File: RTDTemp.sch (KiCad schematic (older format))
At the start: 92 parts, among them J11 Conn_01x02, J4 CAN_In, J5 CAN_Out, U2 Nucleo_L432KC, U3 PDS1-Sx-Sx, U5 ADM3055E, U7 CDSOT23-T24CAN

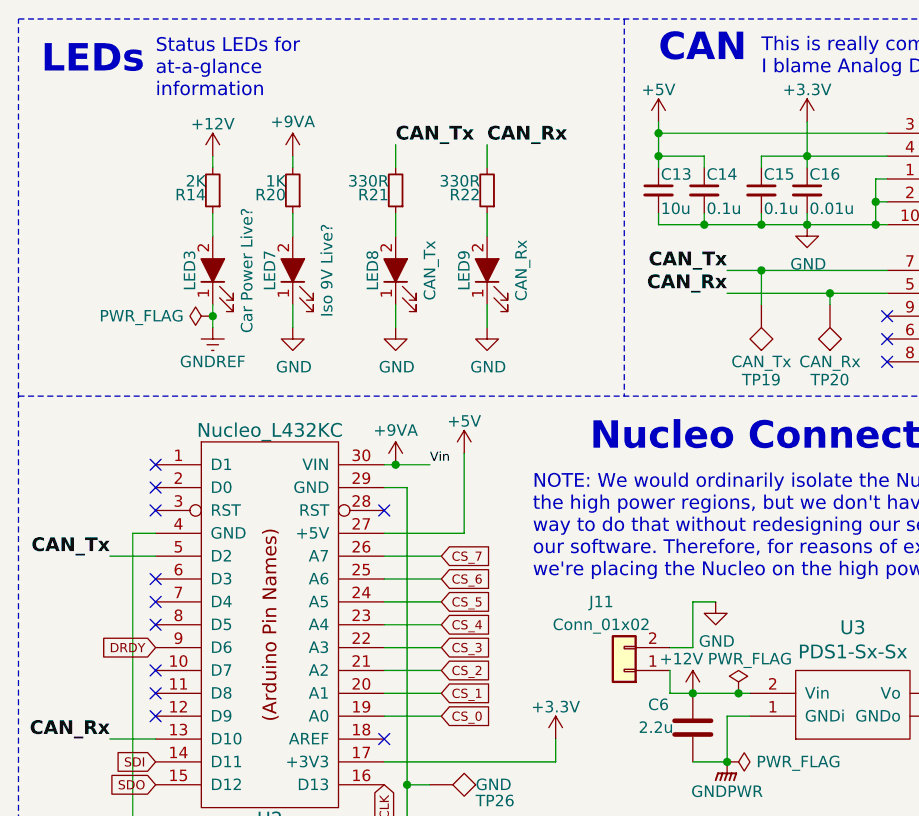
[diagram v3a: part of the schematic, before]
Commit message: Arragned Board
Arragned Board, room for optimization
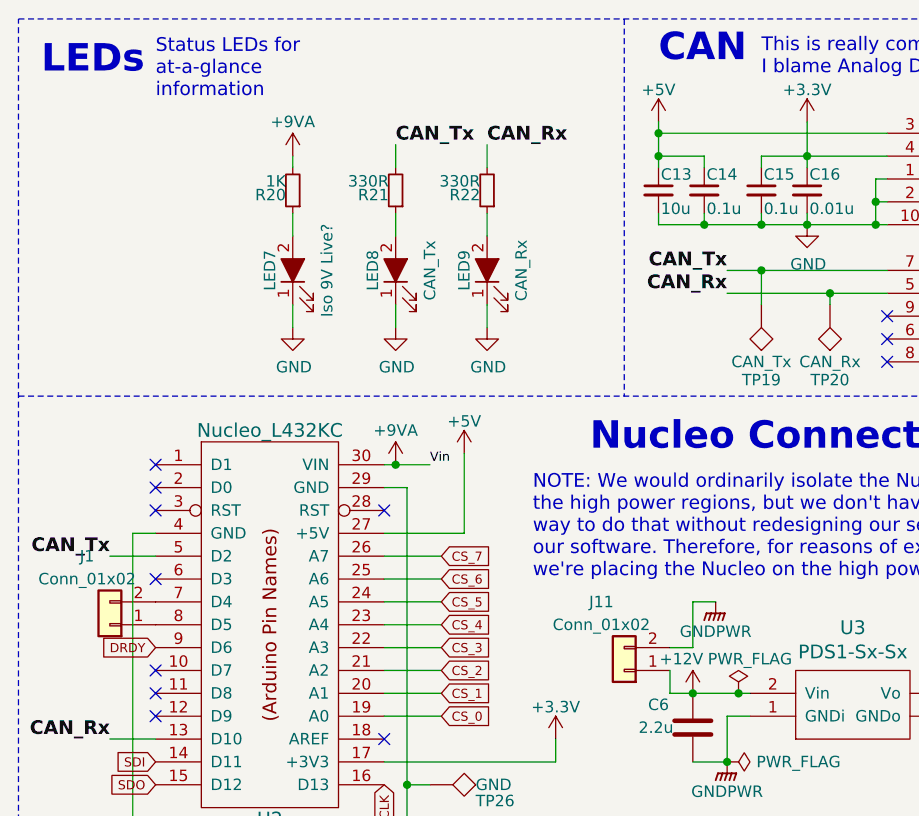
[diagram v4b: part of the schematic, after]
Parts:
- removed LED3: Car Power Live?, LED_SMD:LED_0805_2012Metric, symbol RTDTemp-rescue:LED_ALT-MPPT-rescue
- removed R14: 2K, Resistor_SMD:R_0805_2012Metric, symbol RTDTemp-rescue:R_Small-MPPT-rescue
- added J1: Conn_01x02, Connector_Molex:Molex_Micro-Fit_3.0_43650-0215_1x02_P3.00mm_Vertical, symbol Connector_Generic:Conn_01x02
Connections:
- net GND: no longer J11.2 (Pin_2)
- net GNDPWR: now also J11.2 (Pin_2)
- net at U2.7 (D4): now also J1.2 (Pin_2)
- net at U2.8 (D5): now also J1.1 (Pin_1)
- no-connect marks 15 -> 13
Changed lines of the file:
@@
 Text Label 1000 3700 2    60   ~ 12
 CAN_Rx
-NoConn ~ 1200 2500
-NoConn ~ 1200 2600
 NoConn ~ 1200 3400
 NoConn ~ 1200 3500
@@
 Text Notes 1200 900  0    60   ~ 0
 Status LEDs for\nat-a-glance\ninformation
-$Comp
-L RTDTemp-rescue:LED_ALT-MPPT-rescue LED3
-U 1 1 5BC3DA9B
-P 1450 1650
-F 0 "LED3" H 1450 1750 50  0000 C CNN
-F 1 "Car Power Live?" H 1450 1500 50  0000 C CNN
-F 2 "LED_SMD:LED_0805_2012Metric" H 1450 1650 50  0001 C CNN
-F 3 "" H 1450 1650 50  0001 C CNN
-	1    1450 1650
-	0    -1   -1   0
-$EndComp
-$Comp
-L RTDTemp-rescue:R_Small-MPPT-rescue R14
-U 1 1 5BC3DAA7
-P 1450 1300
-F 0 "R14" H 1480 1320 50  0000 L CNN
-F 1 "2K" H 1480 1260 50  0000 L CNN
-F 2 "Resistor_SMD:R_0805_2012Metric" H 1450 1300 50  0001 C CNN
-F 3 "" H 1450 1300 50  0001 C CNN
-	1    1450 1300
-	-1   0    0    1
-$EndComp
 $Comp
 L RTDTemp-rescue:LED_ALT-MPPT-rescue LED7
@@
 $EndComp
 $Comp
-L RTDTemp-rescue:GNDREF-MPPT-rescue #PWR041
-U 1 1 5BC77E73
-P 1450 1900
-F 0 "#PWR041" H 1450 1650 50  0001 C CNN
-F 1 "GNDREF" H 1450 1750 50  0000 C CNN
-F 2 "" H 1450 1900 50  0001 C CNN
-F 3 "" H 1450 1900 50  0001 C CNN
-	1    1450 1900
-	1    0    0    -1
-$EndComp
-$Comp
-L RTDTemp-rescue:+12V-MPPT-rescue #PWR042
-U 1 1 5BC781A9
-P 1450 1150
-F 0 "#PWR042" H 1450 1000 50  0001 C CNN
-F 1 "+12V" H 1450 1290 50  0000 C CNN
-F 2 "" H 1450 1150 50  0001 C CNN
-F 3 "" H 1450 1150 50  0001 C CNN
-	1    1450 1150
-	1    0    0    -1
-$EndComp
-$Comp
 L RTDTemp-rescue:LED_ALT-MPPT-rescue LED8
 U 1 1 5BC7B329
@@
 	1000 3700 1200 3700
 Wire Wire Line
-	1000 2900 1200 2900
-Wire Wire Line
 	5850 2100 5800 2100
 Wire Wire Line
@@
 	2650 1200 2650 1100
 Wire Wire Line
-	1450 1900 1450 1850
-Wire Wire Line
-	1450 1500 1450 1400
-Wire Wire Line
-	1450 1200 1450 1150
-Wire Wire Line
 	1800 1150 1800 1200
 Wire Wire Line
@@
 Wire Wire Line
 	6150 2100 6200 2100
-$Comp
-L RTDTemp-rescue:Nucleo_L432KC-MPPT-rescue U2
-U 1 1 5BBBD3B0
-P 1700 3200
-F 0 "U2" H 1700 2350 60  0000 C CNN
-F 1 "Nucleo_L432KC" H 1700 4050 60  0000 C CNN
-F 2 "UTSVT_Special:NucleoL432KC" H 1700 2900 60  0001 C CNN
-F 3 "" H 1700 2900 60  0001 C CNN
-	1    1700 3200
-	1    0    0    -1
-$EndComp
 $Comp
 L RTDTemp-rescue:TEST-MPPT-rescue TP26
@@
 Wire Wire Line
 	2450 2900 2200 2900
-$Comp
-L RTDTemp-rescue:PWR_FLAG-MPPT-rescue #FLG0105
-U 1 1 5F3734A8
-P 1450 1850
-F 0 "#FLG0105" H 1450 1925 50  0001 C CNN
-F 1 "PWR_FLAG" V 1450 1977 50  0000 L CNN
-F 2 "" H 1450 1850 50  0001 C CNN
-F 3 "" H 1450 1850 50  0001 C CNN
-	1    1450 1850
-	0    -1   -1   0
-$EndComp
-Connection ~ 1450 1850
-Wire Wire Line
-	1450 1850 1450 1800
 Connection ~ 2300 3900
 Wire Wire Line
@@
 Wire Wire Line
 	5000 3500 5150 3500
-$Comp
-L RTDTemp-rescue:PDS1-Sx-Sx-utsvt-power-regulators U3
-U 1 1 5EB6D889
-P 4250 3550
-F 0 "U3" H 4250 3887 60  0000 C CNN
-F 1 "PDS1-Sx-Sx" H 4250 3781 60  0000 C CNN
-F 2 "UTSVT_ICs:PDSx-S" H 4250 3500 60  0001 C CNN
-F 3 "" H 4250 3500 60  0001 C CNN
-	1    4250 3550
-	1    0    0    -1
-$EndComp
 Connection ~ 4700 3500
 Wire Wire Line
@@
 Wire Wire Line
 	3450 3400 3450 3500
-$Comp
-L power:GND #PWR0103
-U 1 1 5E5C95E9
-P 3650 3100
-F 0 "#PWR0103" H 3650 2850 50  0001 C CNN
-F 1 "GND" H 3655 2927 50  0000 C CNN
-F 2 "" H 3650 3100 50  0001 C CNN
-F 3 "" H 3650 3100 50  0001 C CNN
-	1    3650 3100
-	1    0    0    -1
-$EndComp
-Wire Wire Line
-	1100 2800 1200 2800
 Wire Wire Line
 	1100 4050 1100 2800
 Wire Wire Line
 	2550 2450 2550 2800
-NoConn ~ 1200 2700
 NoConn ~ 2200 2700
 Text Label 1000 2900 2    60   ~ 12
 CAN_Tx
-NoConn ~ 1200 3200
 Wire Wire Line
 	3550 3300 3550 3100
@@
 Text GLabel 1200 3300 0    40   Input ~ 0
 DRDY
-NoConn ~ 1200 3100
 Text GLabel 1200 3800 0    40   Input ~ 0
 SDI
@@
 Text GLabel 2450 2900 2    40   Input ~ 0
 CS_7
-NoConn ~ 1200 3000
 Text GLabel 2450 3000 2    40   Input ~ 0
 CS_6
@@
 Text GLabel 3800 14450 0    40   Input ~ 0
 CS_6
+$Comp
+L RTDTemp-rescue:PDS1-Sx-Sx-utsvt-power-regulators U3
+U 1 1 5EB6D889
+P 4250 3550
+F 0 "U3" H 4250 3887 60  0000 C CNN
+F 1 "PDS1-Sx-Sx" H 4250 3781 60  0000 C CNN
+F 2 "UTSVT_ICs:PDSx-S" H 4250 3500 60  0001 C CNN
+F 3 "" H 4250 3500 60  0001 C CNN
+	1    4250 3550
+	1    0    0    -1
+$EndComp
+$Comp
+L Connector_Generic:Conn_01x02 J1
+U 1 1 5FD57E19
+P 1000 3200
+F 0 "J1" H 1100 2900 50  0000 C CNN
+F 1 "Conn_01x02" H 1100 3000 50  0000 C CNN
+F 2 "Connector_Molex:Molex_Micro-Fit_3.0_43650-0215_1x02_P3.00mm_Vertical" H 1000 3200 50  0001 C CNN
+F 3 "~" H 1000 3200 50  0001 C CNN
+	1    1000 3200
+	-1   0    0    1
+$EndComp
+NoConn ~ 1200 3000
+NoConn ~ 1200 2700
+Wire Wire Line
+	1100 2800 1200 2800
+$Comp
+L RTDTemp-rescue:Nucleo_L432KC-MPPT-rescue U2
+U 1 1 5BBBD3B0
+P 1700 3200
+F 0 "U2" H 1700 2350 60  0000 C CNN
+F 1 "Nucleo_L432KC" H 1700 4050 60  0000 C CNN
+F 2 "UTSVT_Special:NucleoL432KC" H 1700 2900 60  0001 C CNN
+F 3 "" H 1700 2900 60  0001 C CNN
+	1    1700 3200
+	1    0    0    -1
+$EndComp
+Wire Wire Line
+	1000 2900 1200 2900
+NoConn ~ 1200 2500
+NoConn ~ 1200 2600
+$Comp
+L RTDTemp-rescue:GNDPWR-MPPT-rescue #PWR0103
+U 1 1 5FE403E5
+P 3650 3100
+F 0 "#PWR0103" H 3650 2900 50  0001 C CNN
+F 1 "GNDPWR" H 3650 2970 50  0000 C CNN
+F 2 "" H 3650 3050 50  0001 C CNN
+F 3 "" H 3650 3050 50  0001 C CNN
+	1    3650 3100
+	1    0    0    -1
+$EndComp
 $EndSCHEMATC

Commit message: PR ready RTD/Irradiance Sensor Board. Added extra mounts for irradiance I2C and updated power reg to match MPPT. Also cleaner layout.
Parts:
- removed C6: 2.2u, Capacitor_SMD:C_0805_2012Metric, symbol Device:C
- removed C7: 4.7u, Capacitor_SMD:C_0805_2012Metric, symbol Device:C
- removed J11: Conn_01x02, Connector_Molex:Molex_Micro-Fit_3.0_43650-0215_1x02_P3.00mm_Vertical, symbol Connector_Generic:Conn_01x02
- removed RTD0_C0, RTD0_C1, RTD0_C2, RTD1_C0, RTD1_C1, RTD1_C2, RTD2_C0, RTD2_C1, RTD2_C2, RTD3_C0, RTD3_C1, RTD3_C2, RTD4_C0, RTD4_C1, RTD4_C2, RTD5_C0, RTD5_C1, RTD5_C2, RTD6_C0, RTD6_C1, RTD6_C2, RTD7_C0, RTD7_C1, RTD7_C2: 100nF, Capacitor_SMD:C_0805_2012Metric, symbol Device:C_Small
- removed RTD0_J0, RTD1_J0, RTD2_J0, RTD3_J0, RTD4_J0, RTD5_J0, RTD6_J0, RTD7_J0: Conn_01x04, Connector_Molex:Molex_Micro-Fit_3.0_43650-0415_1x04_P3.00mm_Vertical, symbol Connector_Generic:Conn_01x04
- removed RTD0_R0, RTD1_R0, RTD2_R0, RTD3_R0, RTD4_R0, RTD5_R0, RTD6_R0, RTD7_R0: 400, Resistor_SMD:R_0805_2012Metric, symbol Device:R_Small
- removed RTD0_U0, RTD1_U0, RTD2_U0, RTD3_U0, RTD4_U0, RTD5_U0, RTD6_U0, RTD7_U0: MAX31865xAP, Package_SO:SSOP-20_5.3x7.2mm_P0.65mm, symbol Sensor_Temperature:MAX31865xAP
- removed TP26: GND, TestPoint:TestPoint_Keystone_5005-5009_Compact, symbol RTDTemp-rescue:TEST-MPPT-rescue
- removed U3: PDS1-Sx-Sx, UTSVT_ICs:PDSx-S, symbol RTDTemp-rescue:PDS1-Sx-Sx-utsvt-power-regulators
- added C1, C4: 100uF, Capacitor_SMD:C_1210_3225Metric, symbol Device:CP1_Small
- added C2: 47uF, Capacitor_SMD:C_1210_3225Metric, symbol Device:CP1_Small
- added C3: 10uF, Capacitor_SMD:C_0805_2012Metric, symbol Device:C_Small
- added J2: Conn_01x02, Connector_Molex:Molex_Micro-Fit_3.0_43650-0215_1x02_P3.00mm_Vertical, symbol Connector_Generic:Conn_01x02
- added J3: Car Power, Connector_Molex:Molex_Micro-Fit_3.0_43650-0215_1x02_P3.00mm_Vertical, symbol Array:PWR_Connector_43650-0215
- added L1: 4.7uH, Inductor_SMD:L_0805_2012Metric, symbol Device:L_Small
- added LED1: Car Power Live (Green), LED_SMD:LED_0805_2012Metric, symbol Device:LED_ALT
- added LED5: Tracking (Blue), LED_SMD:LED_0805_2012Metric, symbol Device:LED_ALT
- added LED6: Error (Amber), LED_SMD:LED_0805_2012Metric, symbol Device:LED_ALT
- added R1, R2: 4.7k, Resistor_SMD:R_0805_2012Metric, symbol Device:R
- added R3: 1.5K, Resistor_SMD:R_0805_2012Metric, symbol Device:R_Small
- added R7, R8: 330, Resistor_SMD:R_0805_2012Metric, symbol Device:R_Small
- added SW1: SW_Push, Button_Switch_THT:SW_PUSH_6mm, symbol Switch:SW_Push
- added TP2: Car +12V, TestPoint:TestPoint_Keystone_5005-5009_Compact, symbol Connector:TestPoint
- added TP3: Car GND, TestPoint:TestPoint_Keystone_5005-5009_Compact, symbol Connector:TestPoint
- added TP4: +9VA, TestPoint:TestPoint_Keystone_5005-5009_Compact, symbol Connector:TestPoint
- added TP5: GNDP, TestPoint:TestPoint_Keystone_5005-5009_Compact, symbol Connector:TestPoint
- added U2: PWR_REG_PQMC3-Dx-Sx-S, Array-RTDPCB:490_PQMC3_D12_S12_S, symbol Array:PWR_REG_PQMC3-Dx-Sx-S
- C10: renamed from C9; value 10u -> 10uF; symbol RTDTemp-rescue:C_Small-MPPT-rescue -> Device:C_Small
- C11: value 0.1u -> 0.01uF; symbol RTDTemp-rescue:C_Small-MPPT-rescue -> Device:C_Small
- C12: value 0.01u -> 0.1uF; symbol RTDTemp-rescue:C_Small-MPPT-rescue -> Device:C_Small
- C5: renamed from C13; value 10u -> 10uF; symbol RTDTemp-rescue:C_Small-MPPT-rescue -> Device:C_Small
- C6: renamed from C14; value 0.1u -> 0.1uF; symbol RTDTemp-rescue:C_Small-MPPT-rescue -> Device:C_Small
- C7: renamed from C15; value 0.1u -> 0.1uF; symbol RTDTemp-rescue:C_Small-MPPT-rescue -> Device:C_Small
- C8: renamed from C16; value 0.01u -> 0.01uF; symbol RTDTemp-rescue:C_Small-MPPT-rescue -> Device:C_Small
- C9: renamed from C10; value 0.22u -> 0.22uF; symbol RTDTemp-rescue:C_Small-MPPT-rescue -> Device:C_Small
- J4, J5: footprint UTSVT_Connectors:Molex_MicroFit3.0_1x4xP3.00mm_PolarizingPeg_Vertical -> Connector_Molex:Molex_Micro-Fit_3.0_43650-0415_1x04_P3.00mm_Vertical; symbol RTDTemp-rescue:CANConnector-MPPT-rescue -> Array:CAN_Connector_43650-0427
- JP1: symbol RTDTemp-rescue:Jumper_NO_Small-MPPT-rescue -> Device:Jumper_NO_Small
- L2, L3: value 2k -> 1.8kH; symbol RTDTemp-rescue:Ferrite_Bead_Small-MPPT-rescue -> Device:Ferrite_Bead_Small
- LED2: renamed from LED7; value Iso 9V Live? -> Device 9V Live (Green); symbol RTDTemp-rescue:LED_ALT-MPPT-rescue -> Device:LED_ALT
- LED3: renamed from LED9; value CAN_Rx -> CAN_Rx (Blue); symbol RTDTemp-rescue:LED_ALT-MPPT-rescue -> Device:LED_ALT
- LED4: renamed from LED8; value CAN_Tx -> CAN_Tx (Blue); symbol RTDTemp-rescue:LED_ALT-MPPT-rescue -> Device:LED_ALT
- R10: symbol RTDTemp-rescue:R-MPPT-rescue -> Device:R
- R11: renamed from R9; symbol RTDTemp-rescue:R-MPPT-rescue -> Device:R
- R4: renamed from R20; value 1K -> 1.1K; symbol RTDTemp-rescue:R_Small-MPPT-rescue -> Device:R_Small
- R5: renamed from R22; value 330R -> 330; symbol RTDTemp-rescue:R_Small-MPPT-rescue -> Device:R_Small
- R6: renamed from R21; value 330R -> 330; symbol RTDTemp-rescue:R_Small-MPPT-rescue -> Device:R_Small
- R9: renamed from R25; symbol RTDTemp-rescue:R-MPPT-rescue -> Device:R
- TP10: renamed from TP15; symbol RTDTemp-rescue:TEST-MPPT-rescue -> Connector:TestPoint
- TP11: renamed from TP16; symbol RTDTemp-rescue:TEST-MPPT-rescue -> Connector:TestPoint
- TP12: renamed from TP21; symbol RTDTemp-rescue:TEST-MPPT-rescue -> Connector:TestPoint
- TP13: renamed from TP22; symbol RTDTemp-rescue:TEST-MPPT-rescue -> Connector:TestPoint
- TP6: renamed from TP19; symbol RTDTemp-rescue:TEST-MPPT-rescue -> Connector:TestPoint
- TP7: renamed from TP20; symbol RTDTemp-rescue:TEST-MPPT-rescue -> Connector:TestPoint
- TP8: renamed from TP13; symbol RTDTemp-rescue:TEST-MPPT-rescue -> Connector:TestPoint
- TP9: renamed from TP14; symbol RTDTemp-rescue:TEST-MPPT-rescue -> Connector:TestPoint
- U1: renamed from U2; footprint UTSVT_Special:NucleoL432KC -> Array-RTDPCB:MODULE_NUCLEO-L432KC; symbol RTDTemp-rescue:Nucleo_L432KC-MPPT-rescue -> Array:MCU_Nucleo_L432KC
- U3: renamed from U5; footprint UTSVT_ICs:SOIC-20W_7.5x15.4mm_Pitch1.27mm -> Array-RTDPCB:ADM3055EBRIZ; symbol RTDTemp-rescue:ADM3055E-MPPT-rescue -> Array:CAN_Chip_ADM3055E
- U4: renamed from U7; footprint Package_TO_SOT_SMD:SOT-23W_Handsoldering -> Package_TO_SOT_SMD:SOT-23; symbol RTDTemp-rescue:CDSOT23-T24CAN-MPPT-rescue -> Array:CAN_Bus_Protector_CDSOT23-T24CAN
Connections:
- net GND is gone; now on net GNDPWR: C5.2, C6.2, C7.2, C8.2, LED2.1 (K), LED3.1 (K), LED4.1 (K), U1.29 (GND), U1.4 (GND), U3.1 (GND_In), U3.10 (GND_In), U3.2 (GND_In)
- net +12V: now also C1.1, J3.1 (+12V), L1.1, R3.2, TP2.1
- net +3V3: now also R1.2, R2.2
- net +9VA: now also C4.1, TP4.1, U2.6 (+Vo)
- net CS_0: now also U1.20 (A1); no longer U1.19 (A0)
- net CS_1: now also U1.19 (A0); no longer U1.20 (A1)
- net CS_2: now also U1.11 (D8); no longer U1.21 (A2)
- net CS_3: now also U1.12 (D9); no longer U1.22 (A3)
- net CS_4: now also U1.22 (A3); no longer U1.23 (A4)
- net CS_5: now also U1.9 (D6); no longer U1.24 (A5)
- net CS_7: now also U1.6 (D3); no longer U1.26 (A7)
- net DRDY: now also U1.10 (D7); no longer U1.9 (D6)
- net GNDPWR: now also C3.1, C4.2, LED5.1 (K), LED6.1 (K), SW1.2, TP5.1, U2.7 (0V)
- net Reset: now reaches U1.28 (RST)
- net Reset: now also U1.3 (RST), SW1.1
- net at U1.7 (D4): now also J1.1 (Pin_1), J2.1 (Pin_1), R2.1; no longer J1.2 (Pin_2)
- net at U1.8 (D5): now also J1.2 (Pin_2), J2.2 (Pin_2), R1.1; no longer J1.1 (Pin_1)
- net at C11.1, C12.1, J4.1 (5V)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: now also C10.1; no longer C9.1
- net at C11.2, C12.2, J4.2 (GND)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: now also C10.2; no longer C9.2
- net at L2.2, TP8.1, U3.19 (V_ISO_Out): now also C9.1; no longer C10.1
- net at L3.2, TP11.1, U3.18 (GND_ISO_Out)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: now also C9.2; no longer C10.2
- new net: C2.1, L1.2, U2.2 (Vin)
- new net: C3.2, U2.8 (CS)
- new net: LED5.2 (A), R7.1
- new net: LED6.2 (A), R8.1
- new net: LED1.2 (A), R3.1
- new net Error: R8.2, U1.24 (A5)
- new net GNDREF: C1.2, C2.2, J3.2 (GND), LED1.1 (K), TP3.1, U2.1 (GND)
- new net Tracking: R7.2, U1.23 (A4)
- no-connect marks 13 -> 10
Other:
- note added: "Isolated Power Regions:\n* High Power/Nucleo\n - +9A, +5V, +3.3V\n - GNDPWR\n* Low Car Power\n - +12V\n - GNDREF"
- note added: "Note that A7 (PA2) and A2 (PA3) are reserved for STLink UART."
- note added: "Power Regulation"
- note added: "SCL"
- note added: "SDA"
- note removed: "NOTE: We would ordinarily isolate the Nucleo from\nthe high power regions, but we don't have a good\nway to do that without redesigning our sensors and\nour software. Therefore, for reasons of expediency,\nwe're placing the Nucleo on the high power plane."
- moved on the sheet: C10, C11, C12, C5, C6, C7, C8, C9, H1, H2, H3, H4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

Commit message: Addressed review.
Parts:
- TP5: value GNDP -> Device GND
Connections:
- net GNDPWR: now also C1.2, C2.2, J3.2 (GND), LED1.1 (K), TP3.1, U2.1 (GND); no longer C3.1, C4.2, C5.2, C6.2, C7.2, C8.2, LED2.1 (K), LED3.1 (K), LED4.1 (K), LED5.1 (K), LED6.1 (K), SW1.2, TP5.1, U1.29 (GND), U1.4 (GND), U2.7 (0V), U3.1 (GND_In), U3.10 (GND_In), U3.2 (GND_In)
- net GNDREF: now also C3.1, C4.2, C5.2, C6.2, C7.2, C8.2, LED2.1 (K), LED3.1 (K), LED4.1 (K), LED5.1 (K), LED6.1 (K), SW1.2, TP5.1, U1.29 (GND), U1.4 (GND), U2.7 (0V), U3.1 (GND_In), U3.10 (GND_In), U3.2 (GND_In); no longer C1.2, C2.2, J3.2 (GND), LED1.1 (K), TP3.1, U2.1 (GND)
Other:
- note added: "Isolated Power Regions:\n* Device/Board Power\n - +9VA, +5V, +3.3V\n - GNDREF\n* Car Power\n - +12V\n - GNDPWR"
- note removed: "Isolated Power Regions:\n* High Power/Nucleo\n - +9A, +5V, +3.3V\n - GNDPWR\n* Low Car Power\n - +12V\n - GNDREF"
- moved on the sheet: TP3, TP4, TP5

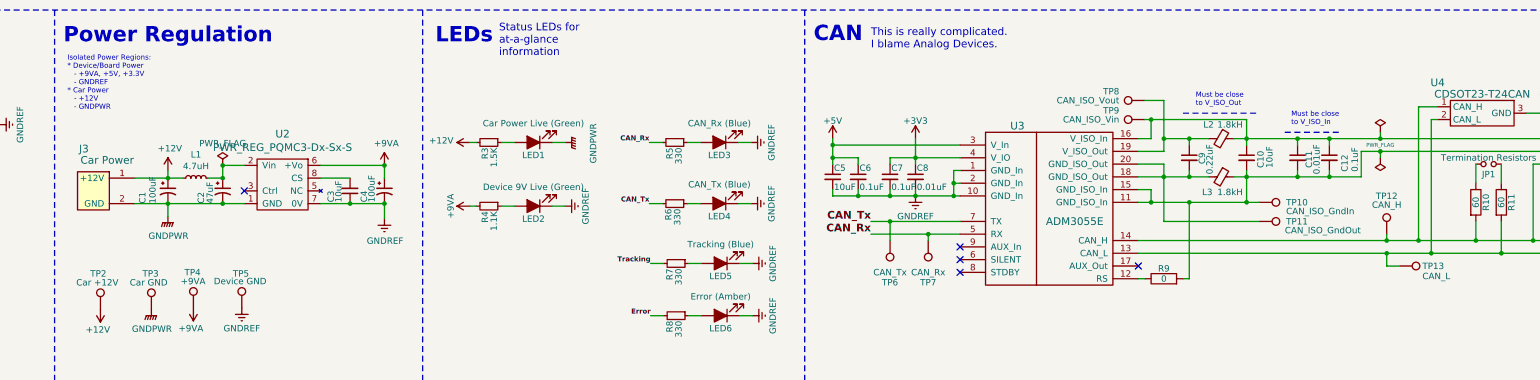
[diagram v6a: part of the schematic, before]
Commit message: Updated README with assembly and testing instructions.
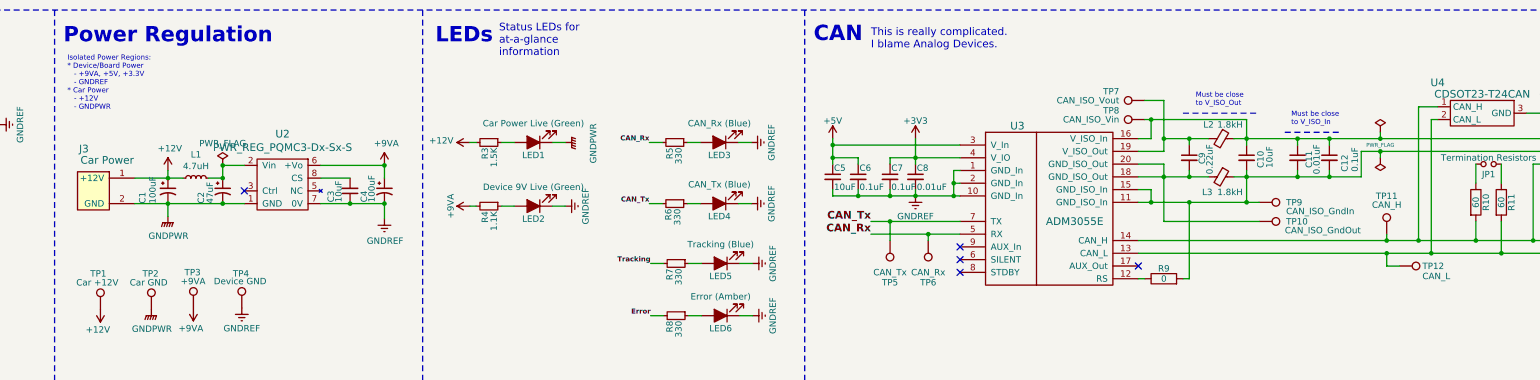
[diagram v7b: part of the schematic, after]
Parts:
- renumbered TP2 to TP1, TP11 to TP10, TP12 to TP11, TP13 to TP12, TP3 to TP2, TP4 to TP3, TP5 to TP4, TP6 to TP5, TP7 to TP6, TP8 to TP7, TP9 to TP8, TP10 to TP9
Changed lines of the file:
@@
 Sheet 1 9
 Title "UT SVT Irradiance/RTD Sensor Board"
-Date "2020-12-07"
+Date "2020-12-13"
 Rev "Rev1.0"
 Comp "UT Solar Vehicle Team"
 Comment1 "Jacob Giddens"
 Comment2 "Matthew Yu"
-Comment3 "Professor Gary Hallock"
+Comment3 "Gary Hallock"
 Comment4 ""
 $EndDescr
@@
 	15620 1610 15620 2210
 $Comp
-L Connector:TestPoint TP13
+L Connector:TestPoint TP12
 U 1 1 5BC9CD87
 P 14270 2610
-F 0 "TP13" V 14300 2790 50  0000 L BNN
+F 0 "TP12" V 14300 2790 50  0000 L BNN
 F 1 "CAN_L" V 14350 2790 50  0000 L CNN
 F 2 "TestPoint:TestPoint_Keystone_5005-5009_Compact" H 14270 2610 50  0001 C CNN
@@
 $EndComp
 $Comp
-L Connector:TestPoint TP12
+L Connector:TestPoint TP11
 U 1 1 5BC9CC23
 P 14170 2360
-F 0 "TP12" H 14170 2630 50  0000 C BNN
+F 0 "TP11" H 14170 2630 50  0000 C BNN
 F 1 "CAN_H" H 14170 2590 50  0000 C CNN
 F 2 "TestPoint:TestPoint_Keystone_5005-5009_Compact" H 14170 2360 50  0001 C CNN
@@
 $EndComp
 $Comp
-L Connector:TestPoint TP6
+L Connector:TestPoint TP5
 U 1 1 5BC87E62
 P 10270 2410
-F 0 "TP6" H 10270 2710 50  0000 C BNN
+F 0 "TP5" H 10270 2710 50  0000 C BNN
 F 1 "CAN_Tx" H 10270 2660 50  0000 C CNN
 F 2 "TestPoint:TestPoint_Keystone_5005-5009_Compact" H 10270 2410 50  0001 C CNN
@@
 $EndComp
 $Comp
-L Connector:TestPoint TP7
+L Connector:TestPoint TP6
 U 1 1 5BC87942
 P 10570 2410
-F 0 "TP7" H 10570 2710 50  0000 C BNN
+F 0 "TP6" H 10570 2710 50  0000 C BNN
 F 1 "CAN_Rx" H 10570 2660 50  0000 C CNN
 F 2 "TestPoint:TestPoint_Keystone_5005-5009_Compact" H 10570 2410 50  0001 C CNN
@@
 $EndComp
 $Comp
-L Connector:TestPoint TP8
+L Connector:TestPoint TP7
 U 1 1 5BC269CB
 P 12270 1310
-F 0 "TP8" V 12370 1510 50  0000 L BNN
+F 0 "TP7" V 12370 1510 50  0000 L BNN
 F 1 "CAN_ISO_Vout" V 12270 1510 50  0000 L CNN
 F 2 "TestPoint:TestPoint_Keystone_5005-5009_Compact" H 12270 1310 50  0001 C CNN
@@
 $EndComp
 $Comp
-L Connector:TestPoint TP10
+L Connector:TestPoint TP9
 U 1 1 5BC242A0
 P 13170 2110
-F 0 "TP10" V 13200 2320 50  0000 L BNN
+F 0 "TP9" V 13200 2320 50  0000 L BNN
 F 1 "CAN_ISO_GndIn" V 13240 2320 50  0000 L CNN
 F 2 "TestPoint:TestPoint_Keystone_5005-5009_Compact" H 13170 2110 50  0001 C CNN
@@
 $EndComp
 $Comp
-L Connector:TestPoint TP11
+L Connector:TestPoint TP10
 U 1 1 5BC2391E
 P 13170 2260
-F 0 "TP11" V 13200 2470 50  0000 L BNN
+F 0 "TP10" V 13200 2470 50  0000 L BNN
 F 1 "CAN_ISO_GndOut" V 13240 2460 50  0000 L CNN
 F 2 "TestPoint:TestPoint_Keystone_5005-5009_Compact" H 13170 2260 50  0001 C CNN
@@
 $EndComp
 $Comp
-L Connector:TestPoint TP9
+L Connector:TestPoint TP8
 U 1 1 5BC226FB
 P 12270 1460
-F 0 "TP9" V 12370 1660 50  0000 L BNN
+F 0 "TP8" V 12370 1660 50  0000 L BNN
 F 1 "CAN_ISO_Vin" V 12270 1660 50  0000 L CNN
 F 2 "TestPoint:TestPoint_Keystone_5005-5009_Compact" H 12270 1460 50  0001 C CNN
@@
 	1050 2670 1220 2670
 $Comp
-L Connector:TestPoint TP2
+L Connector:TestPoint TP1
 U 1 1 608B7F13
 P 4070 2950
-F 0 "TP2" H 3990 3230 50  0000 L CNN
+F 0 "TP1" H 3990 3230 50  0000 L CNN
 F 1 "Car +12V" H 3880 3160 50  0000 L CNN
 F 2 "TestPoint:TestPoint_Keystone_5005-5009_Compact" H 4270 2950 50  0001 C CNN
@@
 $EndComp
 $Comp
-L Connector:TestPoint TP3
+L Connector:TestPoint TP2
 U 1 1 608C010E
 P 4470 2950
-F 0 "TP3" H 4400 3230 50  0000 L CNN
+F 0 "TP2" H 4400 3230 50  0000 L CNN
 F 1 "Car GND" H 4300 3160 50  0000 L CNN
 F 2 "TestPoint:TestPoint_Keystone_5005-5009_Compact" H 4670 2950 50  0001 C CNN
@@
 $EndComp
 $Comp
-L Connector:TestPoint TP4
+L Connector:TestPoint TP3
 U 1 1 608C0667
 P 4800 2940
-F 0 "TP4" H 4730 3220 50  0000 L CNN
+F 0 "TP3" H 4730 3220 50  0000 L CNN
 F 1 "+9VA" H 4700 3150 50  0000 L CNN
 F 2 "TestPoint:TestPoint_Keystone_5005-5009_Compact" H 5000 2940 50  0001 C CNN
@@
 $EndComp
 $Comp
-L Connector:TestPoint TP5
+L Connector:TestPoint TP4
 U 1 1 608C0C20
 P 5180 2940
-F 0 "TP5" H 5110 3210 50  0000 L CNN
+F 0 "TP4" H 5110 3210 50  0000 L CNN
 F 1 "Device GND" H 4960 3150 50  0000 L CNN
 F 2 "TestPoint:TestPoint_Keystone_5005-5009_Compact" H 5380 2940 50  0001 C CNN

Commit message: Added zip and step files
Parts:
- U2: value PWR_REG_PQMC3-Dx-Sx-S -> PWR_REG_PQMC3-D12-S9-S
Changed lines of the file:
@@
 P 5500 1970
 F 0 "U2" H 5500 2367 60  0000 C CNN
-F 1 "PWR_REG_PQMC3-Dx-Sx-S" H 5500 2261 60  0000 C CNN
+F 1 "PWR_REG_PQMC3-D12-S9-S" H 5500 1700 60  0000 C CNN
 F 2 "Array-RTDPCB:490_PQMC3_D12_S12_S" H 5500 2020 60  0001 C CNN
 F 3 "" H 5500 2020 60  0001 C CNN
